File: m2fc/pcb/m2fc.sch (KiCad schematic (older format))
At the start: 70 parts, among them IC101 ADP3335, IC102 STM32F405VGT, IC103 ADP3335, P101 CONN_2, P102 CONN_2, P103 CONN_2, P104 SWD, U101 BAT BOX, U102 ARM SW, U103 HOUSING, U104 HOUSING, U105 HOUSING, U106 MICROSD, U107 MOUNT, U108 MOUNT, U109 MOUNT, U110 MOUNT, U111 MOUNT, U112 MOUNT, X101 8M

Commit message: tidied up
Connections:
- net +BATT: now also P101.1 (P1); no longer P101.2 (PM)
- net GND: now also P101.2 (PM); no longer P101.1 (P1)

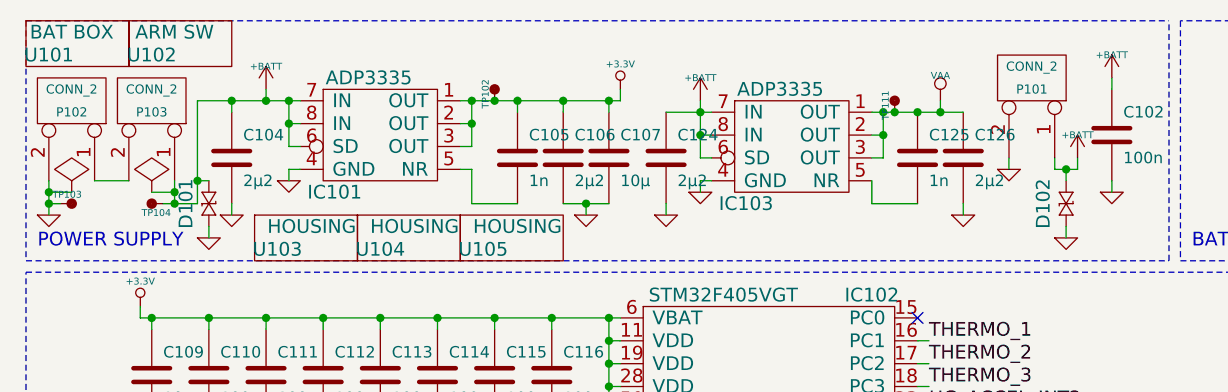
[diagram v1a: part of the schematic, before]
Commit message: flip around power connectors
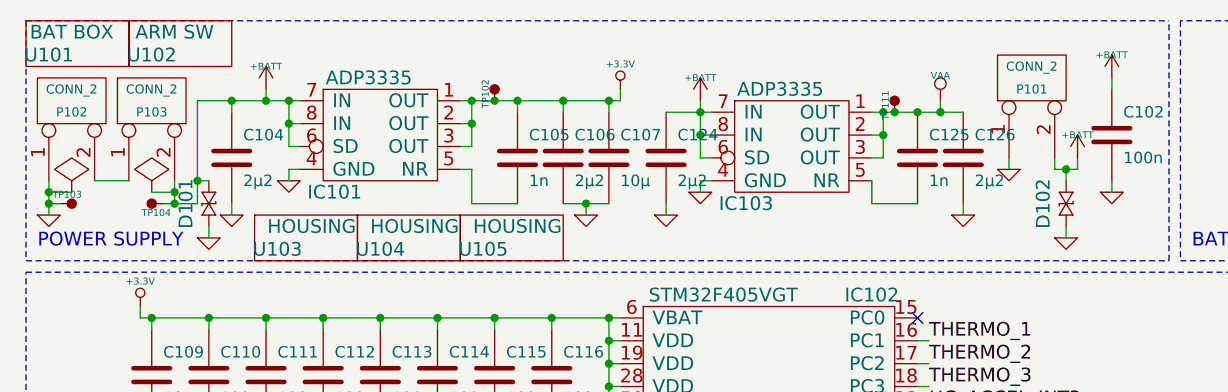
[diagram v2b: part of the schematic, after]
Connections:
- net +BATT: now also P101.2 (PM), P103.2 (PM); no longer P101.1 (P1), P103.1 (P1)
- net GND: now also P101.1 (P1), P102.1 (P1); no longer P101.2 (PM), P102.2 (PM)
- new net: P102.2 (PM), P103.1 (P1)
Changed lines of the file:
@@
 F 4 "1830747" V 700 850 60  0001 C CNN "Farnell"
 	1    700  850
-	0    1    -1   0
+	0    -1   -1   0
 $EndComp
 $Comp
@@
 F 4 "1830747" V 1050 850 60  0001 C CNN "Farnell"
 	1    1050 850
-	0    1    -1   0
+	0    -1   -1   0
 $EndComp
 $Comp
@@
 F 4 "1830747" V 4900 750 60  0001 C CNN "Farnell"
 	1    4900 750
-	0    1    -1   0
-$EndComp
-$Comp
+	0    -1   -1   0
+$EndComp
+$Comp

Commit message: ready to go go go
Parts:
- added U113: LOGO, m2fc:cusf_logo_full, symbol PART
- added U114: LOGO, m2fc:cusf_logo_small, symbol PART

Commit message: final checks, tweaks, etc
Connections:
- net LG_ACCEL_CS: now also IC102.51 (PB12)
- no-connect marks 26 -> 25

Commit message: change sd card part number on m2fc
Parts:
- U106: Farnell 2334075 -> 2358234
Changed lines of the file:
@@
 F 2 "m2fc:MICROSD" H 7450 1750 60  0001 C CNN
 F 3 "" H 7450 1750 60  0000 C CNN
-F 4 "2334075" H 7450 1750 60  0001 C CNN "Farnell"
+F 4 "2358234" H 7450 1750 60  0001 C CNN "Farnell"
 	1    7450 1750
 	1    0    0    -1

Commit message: rescue symbols from m2fc pcb
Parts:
- C101, C102, C103, C104, C105, C106, C107, C108, C109, C110, C111, C112, C113, C114, C115, C116, C117, C118, C119, C120, C121, C122, C123, C124, C125, C126: symbol C -> C-RESCUE-m2fc
- R101, R102, R103, R104, R105, R106, R107, R108: symbol R -> R-RESCUE-m2fc
